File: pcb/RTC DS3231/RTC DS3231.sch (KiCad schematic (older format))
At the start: 14 parts, among them J101 Conn_01x06_Male, J102 Conn_01x04_Male, U101 DS3231M, U102 AT24CS32-SSHM

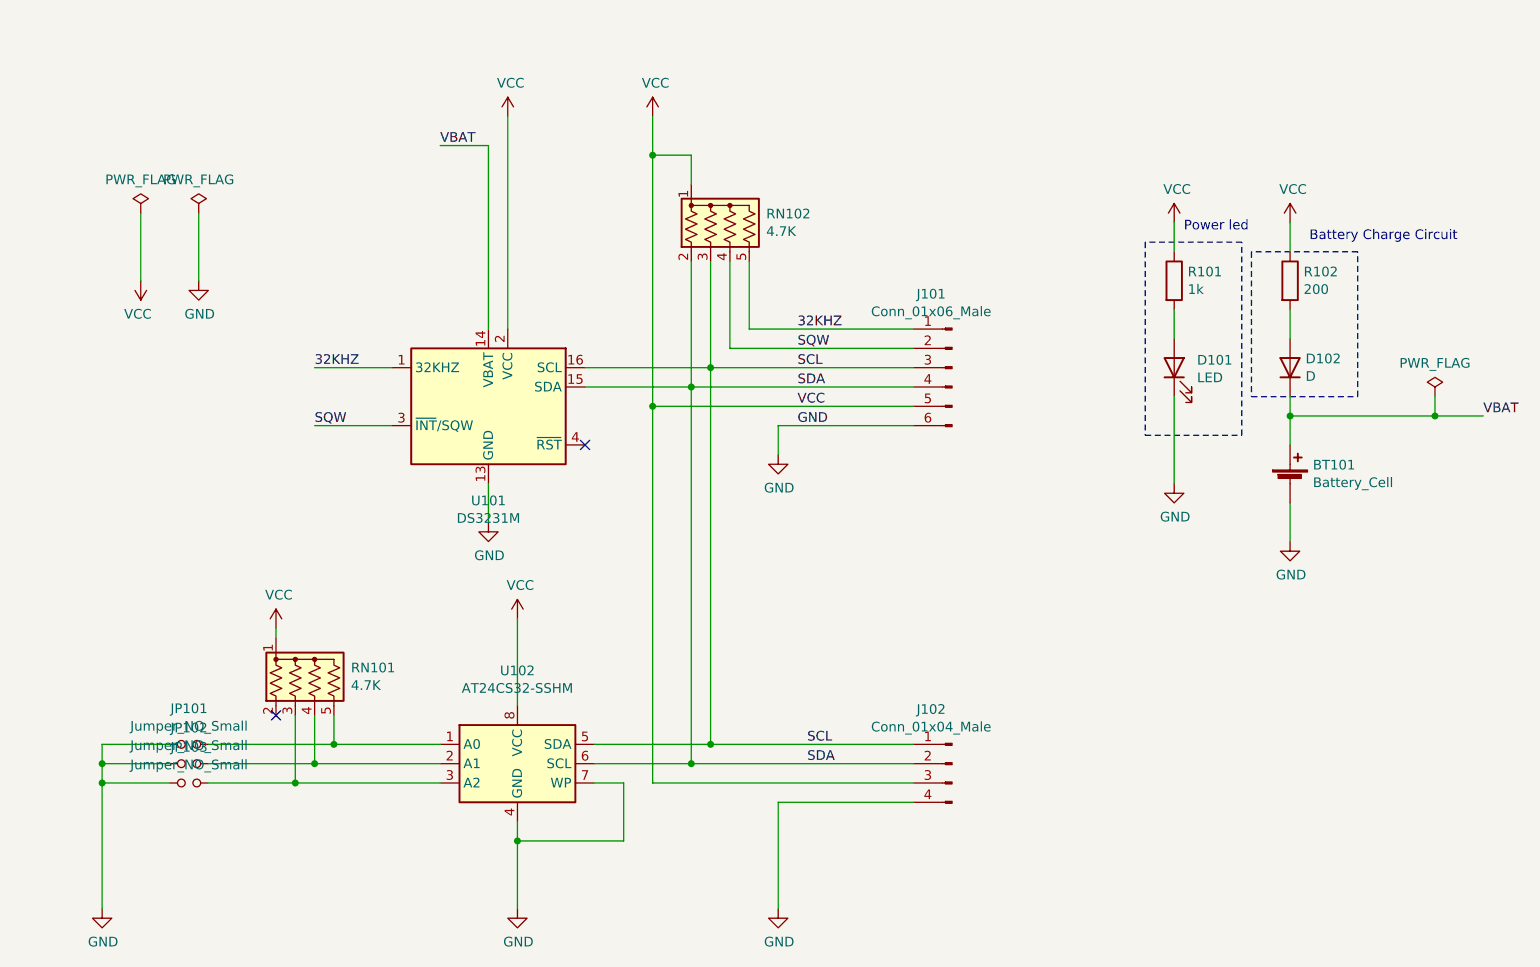
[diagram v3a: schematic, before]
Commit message: Modificación esquemático.
Se agregaron los fiduciales y los recuadros que aclaran a que corresponde cada parte del circuito.
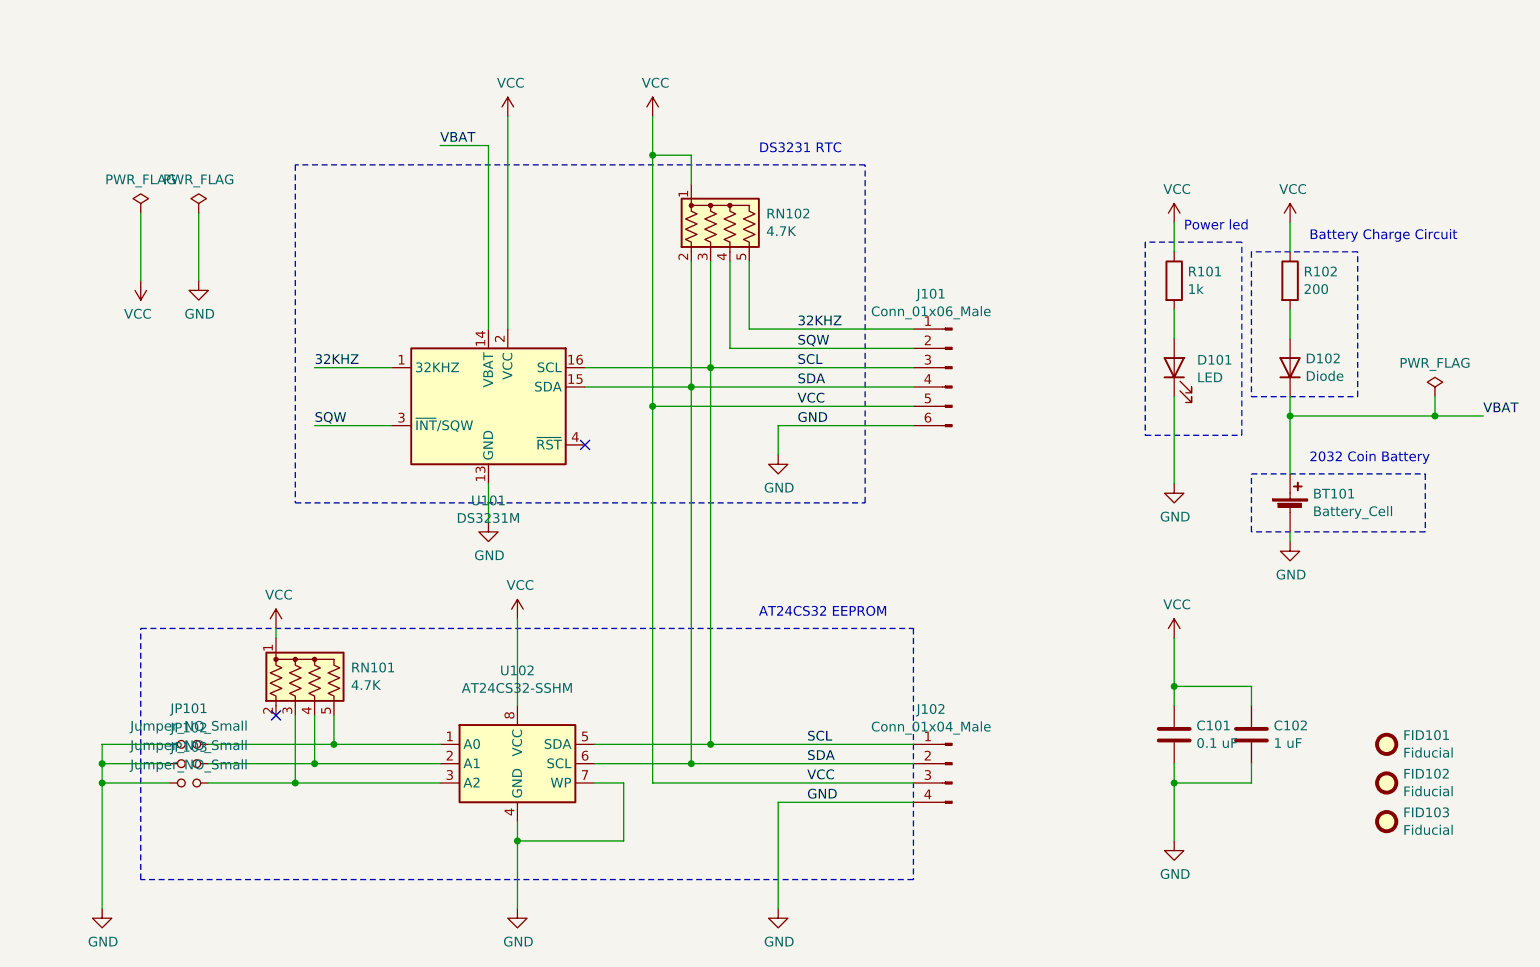
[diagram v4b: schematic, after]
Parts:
- added C101: 0.1 uF, symbol Device:C
- added C102: 1 uF, symbol Device:C
- added FID101, FID102, FID103: Fiducial, symbol Mechanical:Fiducial
- D102: value D -> Diode
- RN101, RN102: footprint Resistor_THT:R_Array_SIP5 -> Resistor_SMD:R_Array_Concave_4x0603
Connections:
- net GND: now also C101.2, C102.2
- net VCC: now also C101.1, C102.1
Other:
- note added: "2032 Coin Battery"
- note added: "AT24CS32 EEPROM"
- note added: "DS3231 RTC"
- moved on the sheet: BT101
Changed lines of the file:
@@
 encoding utf-8
 Sheet 1 1
-Title "RTC DS3231"
+Title "Réplica Módulo RTC DS3231"
 Date "2021-09-14"
 Rev "Version 1"
-Comp ""
-Comment1 ""
+Comp "Author: Matias Meghinasso"
+Comment1 "License: GPL V3.0"
 Comment2 ""
 Comment3 ""
@@
 L Device:Battery_Cell BT101
 U 1 1 61423193
-P 9400 3600
-F 0 "BT101" H 9518 3696 50  0000 L CNN
-F 1 "Battery_Cell" H 9518 3605 50  0000 L CNN
-F 2 "Battery:BatteryHolder_Keystone_1058_1x2032" V 9400 3660 50  0001 C CNN
-F 3 "~" V 9400 3660 50  0001 C CNN
-	1    9400 3600
+P 9400 3750
+F 0 "BT101" H 9518 3846 50  0000 L CNN
+F 1 "Battery_Cell" H 9518 3755 50  0000 L CNN
+F 2 "Battery:BatteryHolder_Keystone_1058_1x2032" V 9400 3810 50  0001 C CNN
+F 3 "~" V 9400 3810 50  0001 C CNN
+	1    9400 3750
 	1    0    0    -1
 $EndComp
@@
 F 0 "RN102" H 6688 2296 50  0000 L CNN
 F 1 "4.7K" H 6688 2205 50  0000 L CNN
-F 2 "Resistor_THT:R_Array_SIP5" V 6775 2250 50  0001 C CNN
+F 2 "Resistor_SMD:R_Array_Concave_4x0603" V 6775 2250 50  0001 C CNN
 F 3 "http://www.vishay.com/docs/31509/csc.pdf" H 6500 2250 50  0001 C CNN
 	1    6500 2250
@@
 	9400 3150 9400 3250
 Wire Wire Line
-	9400 3700 9400 3900
+	9400 3850 9400 3900
 $Comp
 L power:VCC #PWR0107
@@
 P 9400 3000
 F 0 "D102" V 9446 2920 50  0000 R CNN
-F 1 "D" V 9355 2920 50  0000 R CNN
+F 1 "Diode" V 9355 2920 50  0000 R CNN
 F 2 "Diode_SMD:D_0805_2012Metric" H 9400 3000 50  0001 C CNN
 F 3 "~" H 9400 3000 50  0001 C CNN
@@
 Connection ~ 9400 3250
 Wire Wire Line
-	9400 3250 9400 3400
+	9400 3250 9400 3550
 $Comp
 L Device:R R102
@@
 F 0 "RN101" H 4538 4646 50  0000 L CNN
 F 1 "4.7K" H 4538 4555 50  0000 L CNN
-F 2 "Resistor_THT:R_Array_SIP5" V 4625 4600 50  0001 C CNN
+F 2 "Resistor_SMD:R_Array_Concave_4x0603" V 4625 4600 50  0001 C CNN
 F 3 "http://www.vishay.com/docs/31509/csc.pdf" H 4350 4600 50  0001 C CNN
 	1    4350 4600
@@
 Text Notes 8850 2300 0    50   ~ 0
 Power led
+Text Label 6900 5150 0    50   ~ 0
+VCC
+Text Label 6900 5250 0    50   ~ 0
+GND
+$Comp
+L power:VCC #PWR0116
+U 1 1 61563DF1
+P 8800 4400
+F 0 "#PWR0116" H 8800 4250 50  0001 C CNN
+F 1 "VCC" H 8815 4573 50  0000 C CNN
+F 2 "" H 8800 4400 50  0001 C CNN
+F 3 "" H 8800 4400 50  0001 C CNN
+	1    8800 4400
+	1    0    0    -1
+$EndComp
+$Comp
+L power:GND #PWR0117
+U 1 1 6156421C
+P 8800 5450
+F 0 "#PWR0117" H 8800 5200 50  0001 C CNN
+F 1 "GND" H 8805 5277 50  0000 C CNN
+F 2 "" H 8800 5450 50  0001 C CNN
+F 3 "" H 8800 5450 50  0001 C CNN
+	1    8800 5450
+	1    0    0    -1
+$EndComp
+$Comp
+L Device:C C102
+U 1 1 615648EE
+P 9200 4900
+F 0 "C102" H 9315 4946 50  0000 L CNN
+F 1 "1 uF" H 9315 4855 50  0000 L CNN
+F 2 "" H 9238 4750 50  0001 C CNN
+F 3 "~" H 9200 4900 50  0001 C CNN
+	1    9200 4900
+	1    0    0    -1
+$EndComp
+$Comp
+L Device:C C101
+U 1 1 61564D51
+P 8800 4900
+F 0 "C101" H 8915 4946 50  0000 L CNN
+F 1 "0.1 uF" H 8915 4855 50  0000 L CNN
+F 2 "" H 8838 4750 50  0001 C CNN
+F 3 "~" H 8800 4900 50  0001 C CNN
+	1    8800 4900
+	1    0    0    -1
+$EndComp
+Wire Wire Line
+	8800 4400 8800 4650
+Wire Wire Line
+	9200 4750 9200 4650
+Wire Wire Line
+	9200 4650 8800 4650
+Connection ~ 8800 4650
+Wire Wire Line
+	8800 4650 8800 4750
+Wire Wire Line
+	9200 5050 9200 5150
+Wire Wire Line
+	9200 5150 8800 5150
+Wire Wire Line
+	8800 5050 8800 5150
+Connection ~ 8800 5150
+Wire Wire Line
+	8800 5150 8800 5450
+Wire Notes Line
+	4250 3700 7200 3700
+Wire Notes Line
+	7200 3700 7200 1950
+Wire Notes Line
+	7200 1950 4250 1950
+Wire Notes Line
+	4250 1950 4250 3700
+Text Notes 6650 1900 0    50   ~ 0
+DS3231 RTC
+Wire Notes Line
+	3450 4350 7450 4350
+Wire Notes Line
+	7450 4350 7450 5650
+Wire Notes Line
+	7450 5650 3450 5650
+Wire Notes Line
+	3450 5650 3450 4350
+Text Notes 6650 4300 0    50   ~ 0
+AT24CS32 EEPROM
+Wire Notes Line
+	9200 3550 10100 3550
+Wire Notes Line
+	10100 3550 10100 3850
+Wire Notes Line
+	10100 3850 9200 3850
+Wire Notes Line
+	9200 3850 9200 3550
+Text Notes 9500 3500 0    50   ~ 0
+2032 Coin Battery
+$Comp
+L Mechanical:Fiducial FID103
+U 1 1 61580870
+P 9900 5350
+F 0 "FID103" H 9985 5396 50  0000 L CNN
+F 1 "Fiducial" H 9985 5305 50  0000 L CNN
+F 2 "" H 9900 5350 50  0001 C CNN
+F 3 "~" H 9900 5350 50  0001 C CNN
+	1    9900 5350
+	1    0    0    -1
+$EndComp
+$Comp
+L Mechanical:Fiducial FID102
+U 1 1 61580E6C
+P 9900 5150
+F 0 "FID102" H 9985 5196 50  0000 L CNN
+F 1 "Fiducial" H 9985 5105 50  0000 L CNN
+F 2 "" H 9900 5150 50  0001 C CNN
+F 3 "~" H 9900 5150 50  0001 C CNN
+	1    9900 5150
+	1    0    0    -1
+$EndComp
+$Comp
+L Mechanical:Fiducial FID101
+U 1 1 615818A5
+P 9900 4950
+F 0 "FID101" H 9985 4996 50  0000 L CNN
+F 1 "Fiducial" H 9985 4905 50  0000 L CNN
+F 2 "" H 9900 4950 50  0001 C CNN
+F 3 "~" H 9900 4950 50  0001 C CNN
+	1    9900 4950
+	1    0    0    -1
+$EndComp
 $EndSCHEMATC

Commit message: Reordered components.
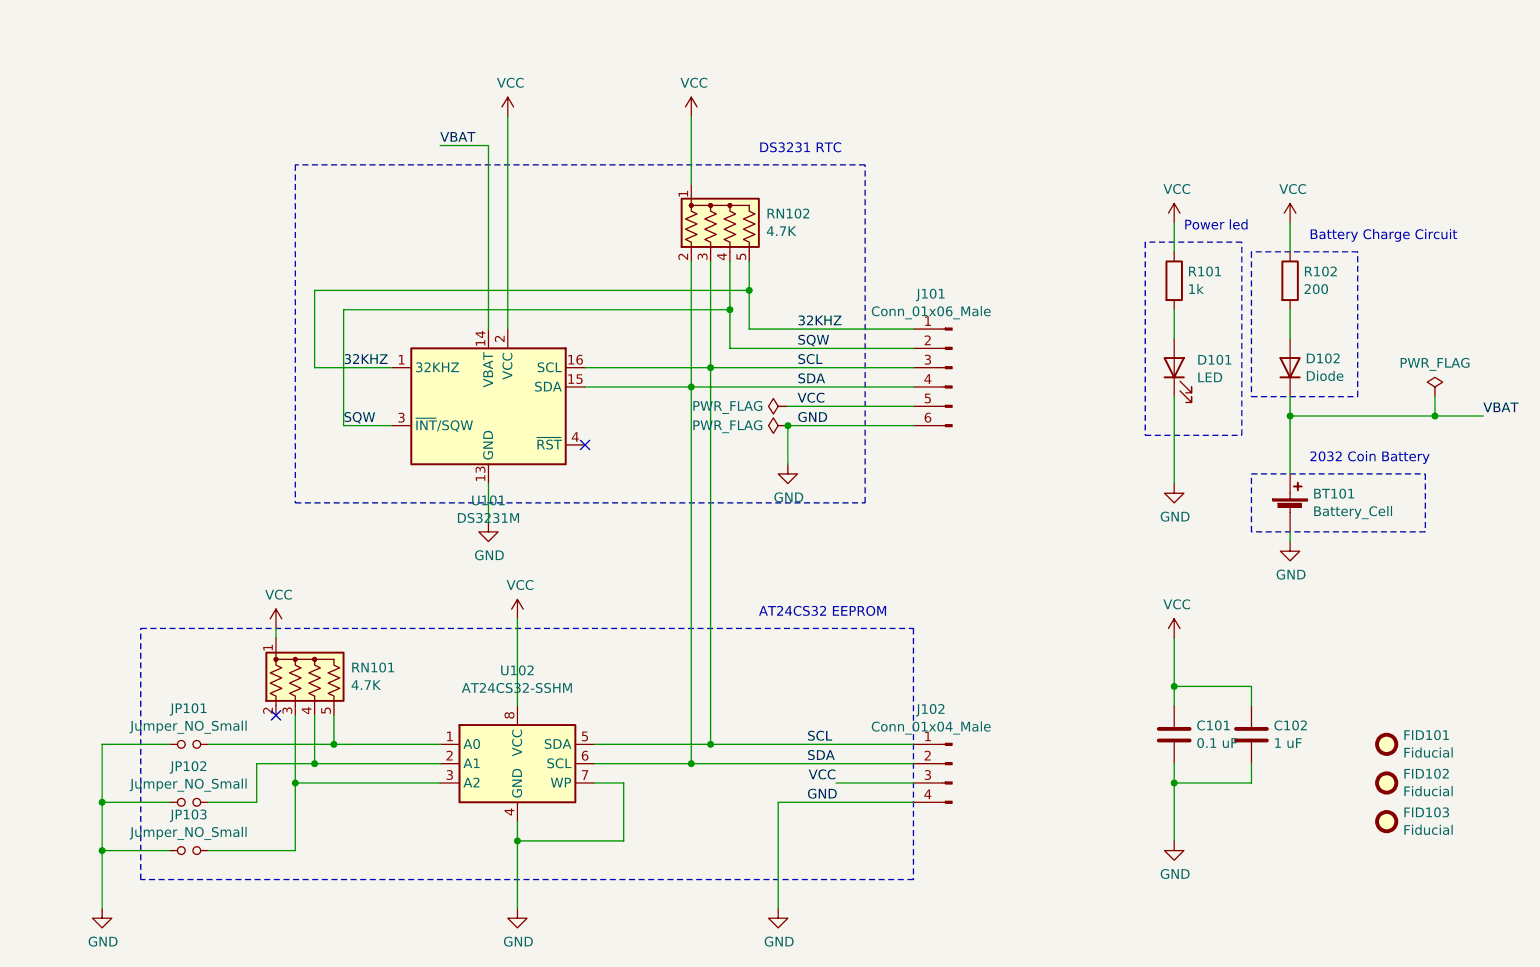
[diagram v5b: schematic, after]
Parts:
- C101, C102: footprint (none) -> Capacitor_SMD:C_0201_0603Metric
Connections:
- net SQW is gone; now on net 32KHZ: J101.2 (Pin_2), RN102.4 (R3), U101.3 (~INT~/SQW)
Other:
- moved on the sheet: JP102, JP103
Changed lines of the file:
@@
 L Device:Jumper_NO_Small JP102
 U 1 1 6142EB82
-P 3700 5050
-F 0 "JP102" H 3700 5235 50  0000 C CNN
-F 1 "Jumper_NO_Small" H 3700 5144 50  0000 C CNN
-F 2 "TestPoint:TestPoint_2Pads_Pitch2.54mm_Drill0.8mm" H 3700 5050 50  0001 C CNN
-F 3 "~" H 3700 5050 50  0001 C CNN
-	1    3700 5050
+P 3700 5250
+F 0 "JP102" H 3700 5435 50  0000 C CNN
+F 1 "Jumper_NO_Small" H 3700 5344 50  0000 C CNN
+F 2 "TestPoint:TestPoint_2Pads_Pitch2.54mm_Drill0.8mm" H 3700 5250 50  0001 C CNN
+F 3 "~" H 3700 5250 50  0001 C CNN
+	1    3700 5250
 	1    0    0    -1
 $EndComp
@@
 L Device:Jumper_NO_Small JP103
 U 1 1 6142EF02
-P 3700 5150
-F 0 "JP103" H 3700 5335 50  0000 C CNN
-F 1 "Jumper_NO_Small" H 3700 5244 50  0000 C CNN
-F 2 "TestPoint:TestPoint_2Pads_Pitch2.54mm_Drill0.8mm" H 3700 5150 50  0001 C CNN
-F 3 "~" H 3700 5150 50  0001 C CNN
-	1    3700 5150
+P 3700 5500
+F 0 "JP103" H 3700 5685 50  0000 C CNN
+F 1 "Jumper_NO_Small" H 3700 5594 50  0000 C CNN
+F 2 "TestPoint:TestPoint_2Pads_Pitch2.54mm_Drill0.8mm" H 3700 5500 50  0001 C CNN
+F 3 "~" H 3700 5500 50  0001 C CNN
+	1    3700 5500
 	1    0    0    -1
 $EndComp
@@
 L power:VCC #PWR0107
 U 1 1 614A0B0F
-P 6100 1700
-F 0 "#PWR0107" H 6100 1550 50  0001 C CNN
-F 1 "VCC" H 6115 1873 50  0000 C CNN
-F 2 "" H 6100 1700 50  0001 C CNN
-F 3 "" H 6100 1700 50  0001 C CNN
-	1    6100 1700
+P 6300 1700
+F 0 "#PWR0107" H 6300 1550 50  0001 C CNN
+F 1 "VCC" H 6315 1873 50  0000 C CNN
+F 2 "" H 6300 1700 50  0001 C CNN
+F 3 "" H 6300 1700 50  0001 C CNN
+	1    6300 1700
 	1    0    0    -1
 $EndComp
@@
 SDA
 Wire Wire Line
-	6600 2450 6600 2800
+	6600 2450 6600 2600
 Wire Wire Line
 	6600 2800 7450 2800
@@
 32KHZ
 Wire Wire Line
-	6500 2450 6500 2900
-Wire Wire Line
 	6500 2900 7450 2900
 Text Label 6850 2900 0    50   ~ 0
 SQW
 Wire Wire Line
-	6300 1900 6300 2050
+	6300 1700 6300 2050
 Wire Wire Line
 	6400 2450 6400 3000
@@
 L power:GND #PWR0108
 U 1 1 614B9641
-P 6750 3450
-F 0 "#PWR0108" H 6750 3200 50  0001 C CNN
-F 1 "GND" H 6755 3277 50  0000 C CNN
-F 2 "" H 6750 3450 50  0001 C CNN
-F 3 "" H 6750 3450 50  0001 C CNN
-	1    6750 3450
-	1    0    0    -1
-$EndComp
-Wire Wire Line
-	6750 3300 6750 3450
-Wire Wire Line
-	6100 3200 7450 3200
-Wire Wire Line
-	6300 1900 6100 1900
-Connection ~ 6100 1900
-Wire Wire Line
-	6100 1900 6100 3200
-Wire Wire Line
-	6750 3300 7450 3300
+P 6800 3500
+F 0 "#PWR0108" H 6800 3250 50  0001 C CNN
+F 1 "GND" H 6805 3327 50  0000 C CNN
+F 2 "" H 6800 3500 50  0001 C CNN
+F 3 "" H 6800 3500 50  0001 C CNN
+	1    6800 3500
+	1    0    0    -1
+$EndComp
+Wire Wire Line
+	6800 3300 6800 3500
+Wire Wire Line
+	6800 3200 7450 3200
+Wire Wire Line
+	6800 3300 7450 3300
 Wire Wire Line
 	4150 4350 4150 4400
@@
 	-1   0    0    -1
 $EndComp
-Text Label 4350 3000 0    50   ~ 0
-32KHZ
-Text Label 4350 3300 0    50   ~ 0
+Text Label 4500 3300 0    50   ~ 0
 SQW
 Wire Wire Line
@@
 	5000 1850 5250 1850
 Wire Wire Line
-	4750 3000 4350 3000
-Wire Wire Line
-	4750 3300 4350 3300
-Wire Wire Line
-	6100 3200 6100 5150
-Wire Wire Line
-	6100 5150 7450 5150
-Connection ~ 6100 3200
+	4750 3300 4500 3300
+Wire Wire Line
+	7050 5150 7450 5150
 $Comp
 L power:GND #PWR0109
@@
 	4450 4950 3800 4950
 Connection ~ 4450 4950
-Wire Wire Line
-	3800 5050 4350 5050
-Connection ~ 4350 5050
-Wire Wire Line
-	4250 5150 3800 5150
-Connection ~ 4250 5150
 $Comp
 L power:GND #PWR0101
@@
 	3600 4950 3250 4950
 Wire Wire Line
-	3600 5150 3250 5150
-Connection ~ 3250 5150
-Wire Wire Line
-	3250 5150 3250 5800
-Wire Wire Line
-	3250 4950 3250 5050
-Wire Wire Line
-	3250 5050 3600 5050
-Connection ~ 3250 5050
-Wire Wire Line
-	3250 5050 3250 5150
-Wire Wire Line
 	5800 5150 5950 5150
 Wire Wire Line
@@
 	1    0    0    -1
 $EndComp
-Wire Wire Line
-	6100 1700 6100 1900
-Text Label 6850 3200 0    50   ~ 0
-VCC
 Text Label 6850 3300 0    50   ~ 0
 GND
@@
 L power:PWR_FLAG #FLG0101
 U 1 1 6153FCF3
-P 3450 2200
-F 0 "#FLG0101" H 3450 2275 50  0001 C CNN
-F 1 "PWR_FLAG" H 3450 2373 50  0000 C CNN
-F 2 "" H 3450 2200 50  0001 C CNN
-F 3 "~" H 3450 2200 50  0001 C CNN
-	1    3450 2200
-	1    0    0    -1
-$EndComp
-$Comp
-L power:VCC #PWR0114
-U 1 1 6154015D
-P 3450 2550
-F 0 "#PWR0114" H 3450 2400 50  0001 C CNN
-F 1 "VCC" H 3465 2723 50  0000 C CNN
-F 2 "" H 3450 2550 50  0001 C CNN
-F 3 "" H 3450 2550 50  0001 C CNN
-	1    3450 2550
-	-1   0    0    1
-$EndComp
-Wire Wire Line
-	3450 2200 3450 2550
-$Comp
-L power:GND #PWR0115
-U 1 1 615482DE
-P 3750 2550
-F 0 "#PWR0115" H 3750 2300 50  0001 C CNN
-F 1 "GND" H 3755 2377 50  0000 C CNN
-F 2 "" H 3750 2550 50  0001 C CNN
-F 3 "" H 3750 2550 50  0001 C CNN
-	1    3750 2550
-	1    0    0    -1
+P 6800 3200
+F 0 "#FLG0101" H 6800 3275 50  0001 C CNN
+F 1 "PWR_FLAG" V 6800 3327 50  0000 L CNN
+F 2 "" H 6800 3200 50  0001 C CNN
+F 3 "~" H 6800 3200 50  0001 C CNN
+	1    6800 3200
+	0    -1   -1   0
 $EndComp
 $Comp
 L power:PWR_FLAG #FLG0102
 U 1 1 615486C4
-P 3750 2200
-F 0 "#FLG0102" H 3750 2275 50  0001 C CNN
-F 1 "PWR_FLAG" H 3750 2373 50  0000 C CNN
-F 2 "" H 3750 2200 50  0001 C CNN
-F 3 "~" H 3750 2200 50  0001 C CNN
-	1    3750 2200
-	1    0    0    -1
-$EndComp
-Wire Wire Line
-	3750 2200 3750 2550
+P 6800 3300
+F 0 "#FLG0102" H 6800 3375 50  0001 C CNN
+F 1 "PWR_FLAG" V 6800 3427 50  0000 L CNN
+F 2 "" H 6800 3300 50  0001 C CNN
+F 3 "~" H 6800 3300 50  0001 C CNN
+	1    6800 3300
+	0    -1   -1   0
+$EndComp
 $Comp
 L power:PWR_FLAG #FLG0103
@@
 Text Notes 8850 2300 0    50   ~ 0
 Power led
-Text Label 6900 5150 0    50   ~ 0
+Text Label 7050 5150 2    50   ~ 0
 VCC
 Text Label 6900 5250 0    50   ~ 0
@@
 F 0 "C102" H 9315 4946 50  0000 L CNN
 F 1 "1 uF" H 9315 4855 50  0000 L CNN
-F 2 "" H 9238 4750 50  0001 C CNN
+F 2 "Capacitor_SMD:C_0201_0603Metric" H 9238 4750 50  0001 C CNN
 F 3 "~" H 9200 4900 50  0001 C CNN
 	1    9200 4900
@@
 F 0 "C101" H 8915 4946 50  0000 L CNN
 F 1 "0.1 uF" H 8915 4855 50  0000 L CNN
-F 2 "" H 8838 4750 50  0001 C CNN
+F 2 "Capacitor_SMD:C_0201_0603Metric" H 8838 4750 50  0001 C CNN
 F 3 "~" H 8800 4900 50  0001 C CNN
 	1    8800 4900
@@
 	1    0    0    -1
 $EndComp
+Wire Wire Line
+	4350 3000 4350 2600
+Wire Wire Line
+	4350 2600 6600 2600
+Connection ~ 6600 2600
+Wire Wire Line
+	6600 2600 6600 2800
+Text Label 4500 3000 0    50   ~ 0
+32KHZ
+Wire Wire Line
+	6500 2450 6500 2700
+Wire Wire Line
+	4500 2700 6500 2700
+Connection ~ 6500 2700
+Wire Wire Line
+	6500 2700 6500 2900
+Wire Wire Line
+	4350 3000 4750 3000
+Wire Wire Line
+	4500 2700 4500 3300
+Text Label 6850 3200 0    50   ~ 0
+VCC
+Connection ~ 6800 3300
+Wire Wire Line
+	4250 5150 4250 5500
+Wire Wire Line
+	4250 5500 3800 5500
+Connection ~ 4250 5150
+Wire Wire Line
+	3600 5500 3250 5500
+Connection ~ 3250 5500
+Wire Wire Line
+	3250 5500 3250 5800
+Wire Wire Line
+	3250 4950 3250 5250
+Wire Wire Line
+	4350 5050 4050 5050
+Wire Wire Line
+	4050 5050 4050 5250
+Wire Wire Line
+	4050 5250 3800 5250
+Connection ~ 4350 5050
+Wire Wire Line
+	3600 5250 3250 5250
+Connection ~ 3250 5250
+Wire Wire Line
+	3250 5250 3250 5500
 $EndSCHEMATC
